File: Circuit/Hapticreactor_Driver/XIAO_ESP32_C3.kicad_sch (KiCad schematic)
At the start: 5 parts, among them U1 XIAO ESP32C3

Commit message: ハプティックリアクタ用基板完成
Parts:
- R6: value R -> 1k
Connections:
- net D7/GPIO20 is gone; now on net D6/GPIO6: R6.1
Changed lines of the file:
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@@
 		)
 	)
-	(label "D7{slash}GPIO20"
-		(at 195.58 64.77 0)
+	(label "D6{slash}GPIO6"
+		(at 195.58 64.77 180)
 		(effects
 			(font
 				(size 1.27 1.27)
 			)
-			(justify left bottom)
+			(justify right bottom)
 		)
 	)
@@
 			)
 		)
-		(property "Value" "R"
+		(property "Value" "1k"
 			(at 198.12 69.8499 0)
 			(effects

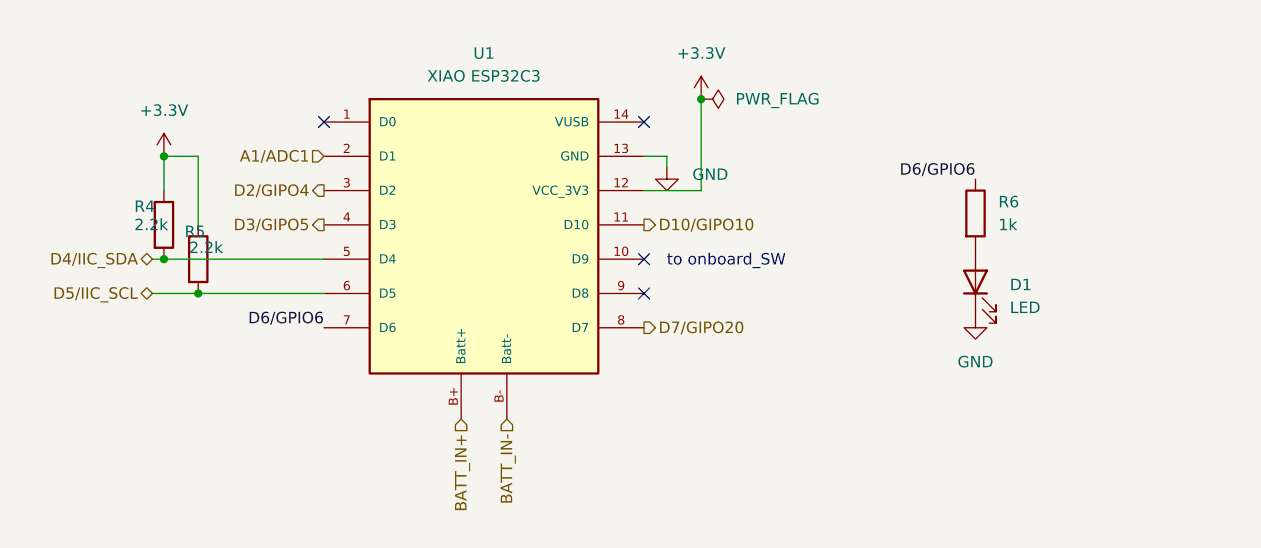
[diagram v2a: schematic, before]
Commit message: 秋野の回路に昇圧DCDCつけて東芝MDつけた
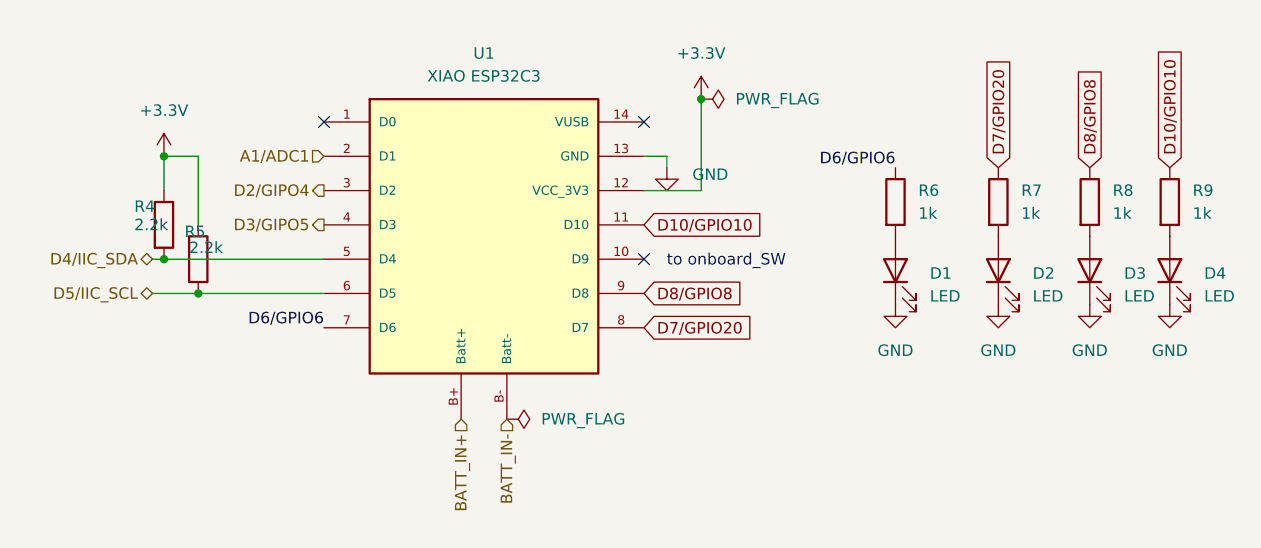
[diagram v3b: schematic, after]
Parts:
- added D2, D3, D4: LED, LED_SMD:LED_0603_1608Metric, symbol Device:LED
- added R7, R8, R9: 1k, Resistor_SMD:R_0603_1608Metric_Pad0.98x0.95mm_HandSolder, symbol Device:R
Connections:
- net GND: now also D2.1 (K), D3.1 (K), D4.1 (K)
- net D8/GPIO8: now reaches U1.9 (D8)
- net D8/GPIO8: now also R8.1
- net D10/GIPO10 renamed D10/GPIO10
- net D10/GPIO10: now also R9.1
- net D7/GIPO20 renamed D7/GPIO20
- net D7/GPIO20: now also R7.1
- new net: D4.2 (A), R9.2
- new net: D3.2 (A), R8.2
- new net: D2.2 (A), R7.2
- no-connect marks 4 -> 3
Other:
- moved on the sheet: D1, R6
